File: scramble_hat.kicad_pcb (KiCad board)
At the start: 4 copper layers, 51.4 x 21.1 mm, 78 parts, among them J1 NCJ6FA-H, J2 TRRS PJ-3X4S (CTIA, bottom-si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, J3 Carrier LEFT 1-7, J4 Carrier RIGHT 1-7, J5 VDD_PoE / PGND, J6 I2C 3V3/AGND/SDA/SCL, J7 TO EURORACK MODULE (alt. to J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, K1 KAQY214S, K2 KAQY214S, Q1 DMP3098 (P-FET 60V), SW1 SS-12D00-G3, U1 ES8389, U2 TPS7A2033, U3 TLV9061, U4 74HC4053

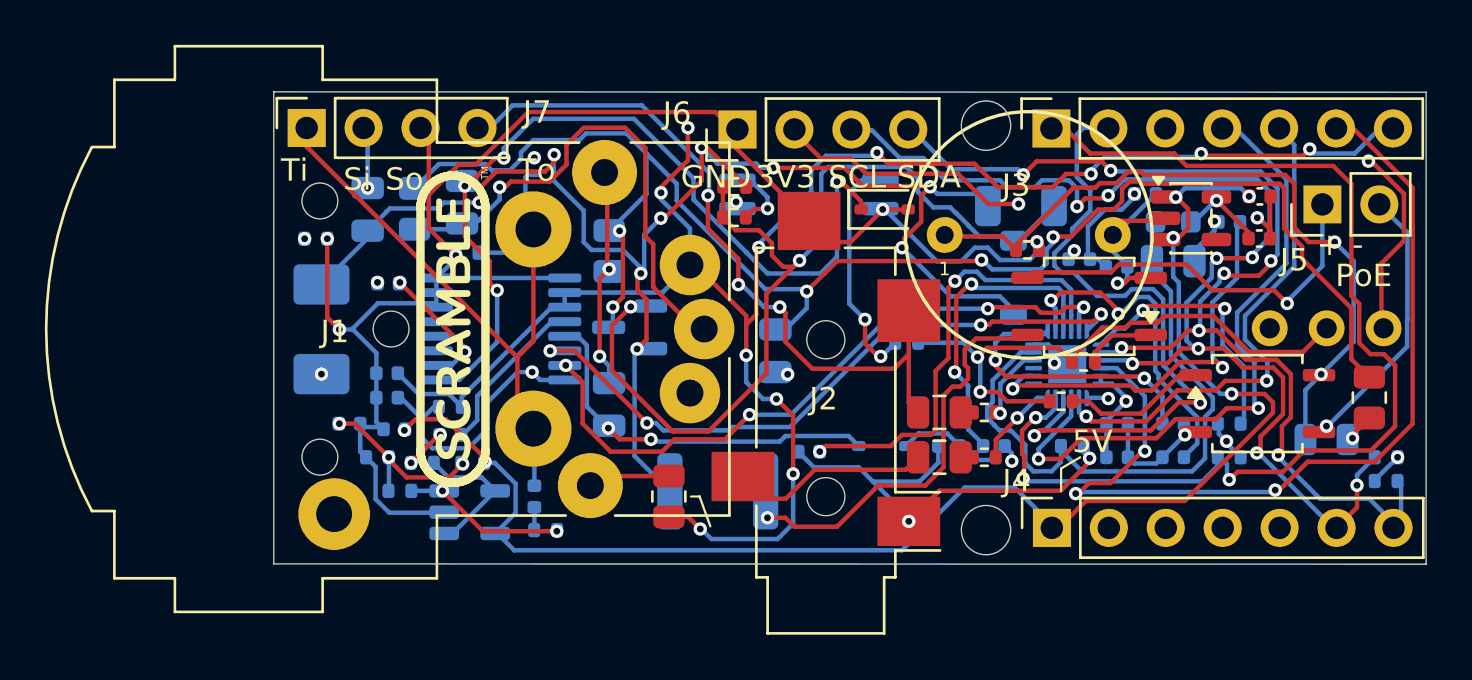
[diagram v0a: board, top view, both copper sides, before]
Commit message: pcb: input-corridor tweaks; J6 display header now DNP; regen fab + docs
- J6 hand-fit per build; eurorack builds don't need it at all (the
  Synthia interposer drives the display directly from its own socket)
- BOM: J6 marked DNP; fab assembly split updated (JLC THT = J3/J4 only;
  CPL 69 placed, 9 exclusions: C19 J1 J2 J5 J6 J7 R14 R27 SW1)
- restore exclude_from_pos flags wiped by layout sessions
- README: power/host notes (USB-C + PoE concurrency, hot-plug pop,
  USB-only bench), brackets/ and docs/ in repo layout
- regen gerbers/BOM/CPL, doc PDFs, board STEP
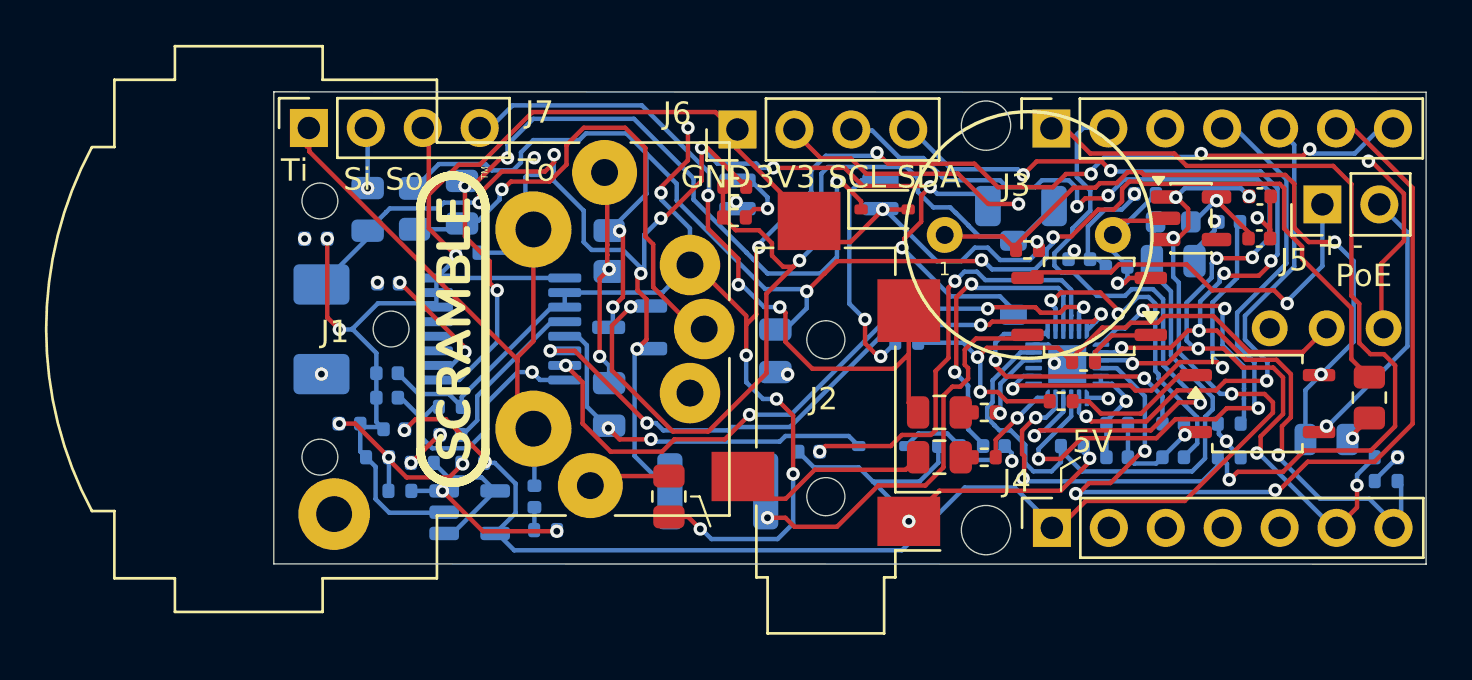
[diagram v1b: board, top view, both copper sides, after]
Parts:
- moved J7 0.10 mm to (82.4, 81.8)
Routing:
- net GTIP: track 30.1 -> 31.0 mm

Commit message: sch+pcb: dual-host mezzanine pinout (ESP32-P4 + Pico) — I2C to J3.1/2, BCLK/LRCK adjacent, MCLK/DET on J4.6/7, new R28 MCLK series link; regen fab + docs; add pinout graphic
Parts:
- added R28: 0R (MCLK link), Resistor_SMD:R_0805_2012Metric, F.Cu at (128.5, 97.2)
- moved R2 29.2 mm to (103.0, 86.8)
- moved R1 27.7 mm to (105.0, 86.8)
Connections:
- J3 pad 1: ASDOUT -> SDA
- J3 pad 2: LRCK -> SCL
- J3 pad 6: MCLK -> LRCK
- J3 pad 7: DET -> ASDOUT
- J4 pad 6: SCL -> MCLK
- J4 pad 7: SDA -> DET
- U1 pad 4: MCLK -> MCLK_C
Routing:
- net MCLK: track 40.2 -> 2.87 mm, vias 3 -> 0
- net MCLK_C: track 0.00 -> 13.7 mm, vias 0 -> 3
- net ASDOUT: track 50.0 -> 38.3 mm
- net LRCK: track 29.9 -> 38.9 mm, vias 2 -> 3
- net SDA: track 49.3 -> 41.8 mm
- net DET: track 80.8 -> 73.9 mm, vias 11 -> 6
- net SCL: track 52.7 -> 46.4 mm, vias 8 -> 6
- net +3V3: track 52.3 -> 56.9 mm
- net MIC1N_XLR: track 38.2 -> 36.1 mm
- net +5V: track 65.8 -> 67.5 mm
- net ADCVREF: track 15.0 -> 13.9 mm
- net V_FILT: track 64.8 -> 65.8 mm
- net MIC1N: track 29.8 -> 30.6 mm
- net TAP_HV: track 17.6 -> 17.1 mm
- net Q1_GATE: track 41.2 -> 40.7 mm

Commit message: pcb: silkscreen tidy-up; remove vestigial V_FILT stub near J1 R pad (cleared clearance error); regen fab + silk PDFs
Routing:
- net V_FILT: track 65.8 -> 64.8 mm
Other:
- board text added: "MCLK JP"
- board text added: "R0 here if hardwired"
- board text added: "XLR"
- board text added: "iS"
- board text added: "iT"
- board text added: "oS"
- board text added: "oT"
- board text removed: "1/4{dblquote} +XLR"
- board text removed: "Si"
- board text removed: "So"
- board text removed: "Ti"
- board text removed: "To"
